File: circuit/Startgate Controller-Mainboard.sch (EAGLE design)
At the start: 22 parts, among them IC1 MAX3490ESA, IC2 L293D, U2 HEF4066BT, U3 HEF4066BT, U4 HEF4066BT, U5 HEF4066BT, X1 RJ45-8L21-B

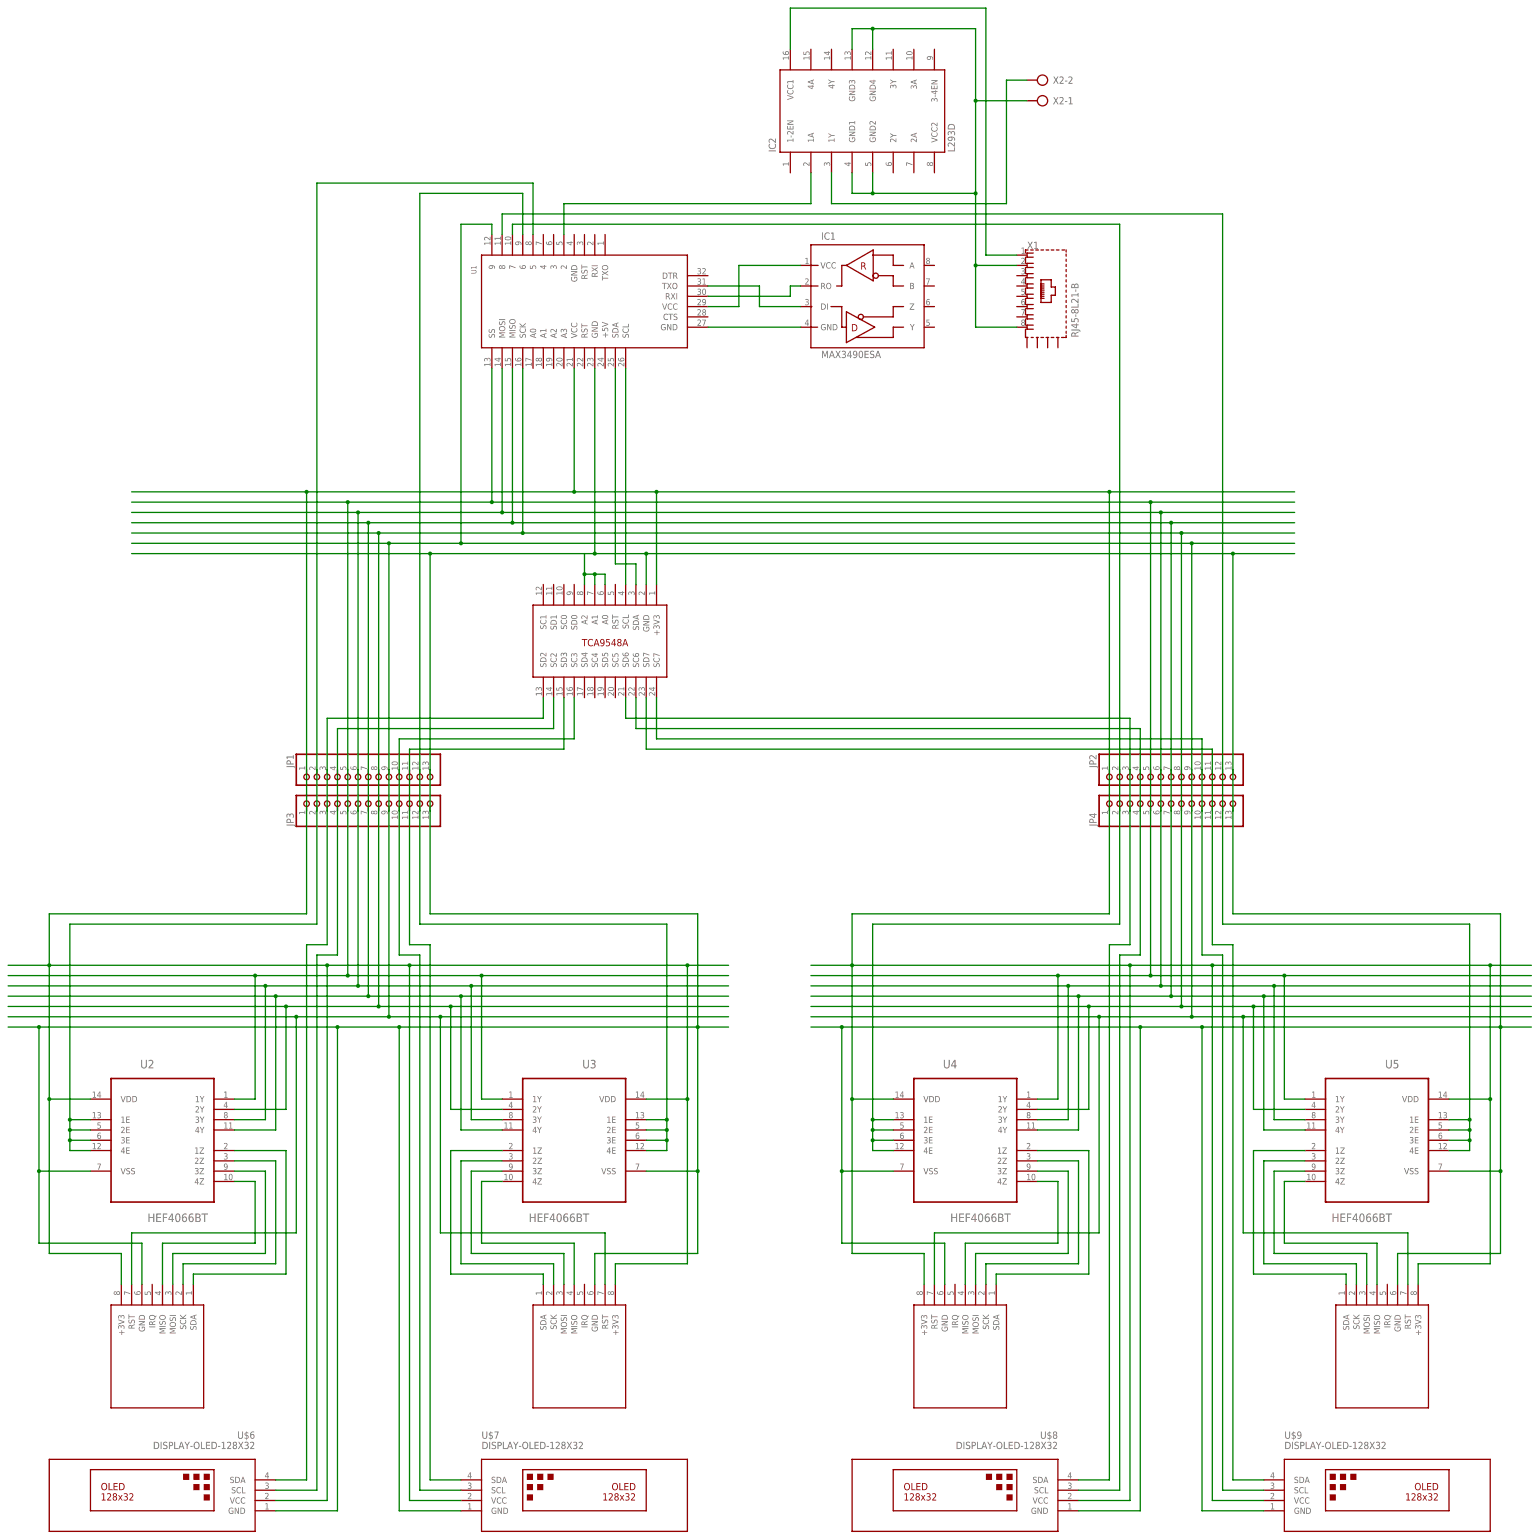
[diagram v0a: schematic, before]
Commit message: add the circuitry for the startgate main- and daughterboards
The main startgate controller has been split up into main board
and daughterboards, to make it easier to send them to the board house.
The two daughterboards should be identical, so the next iteration will
skip one.
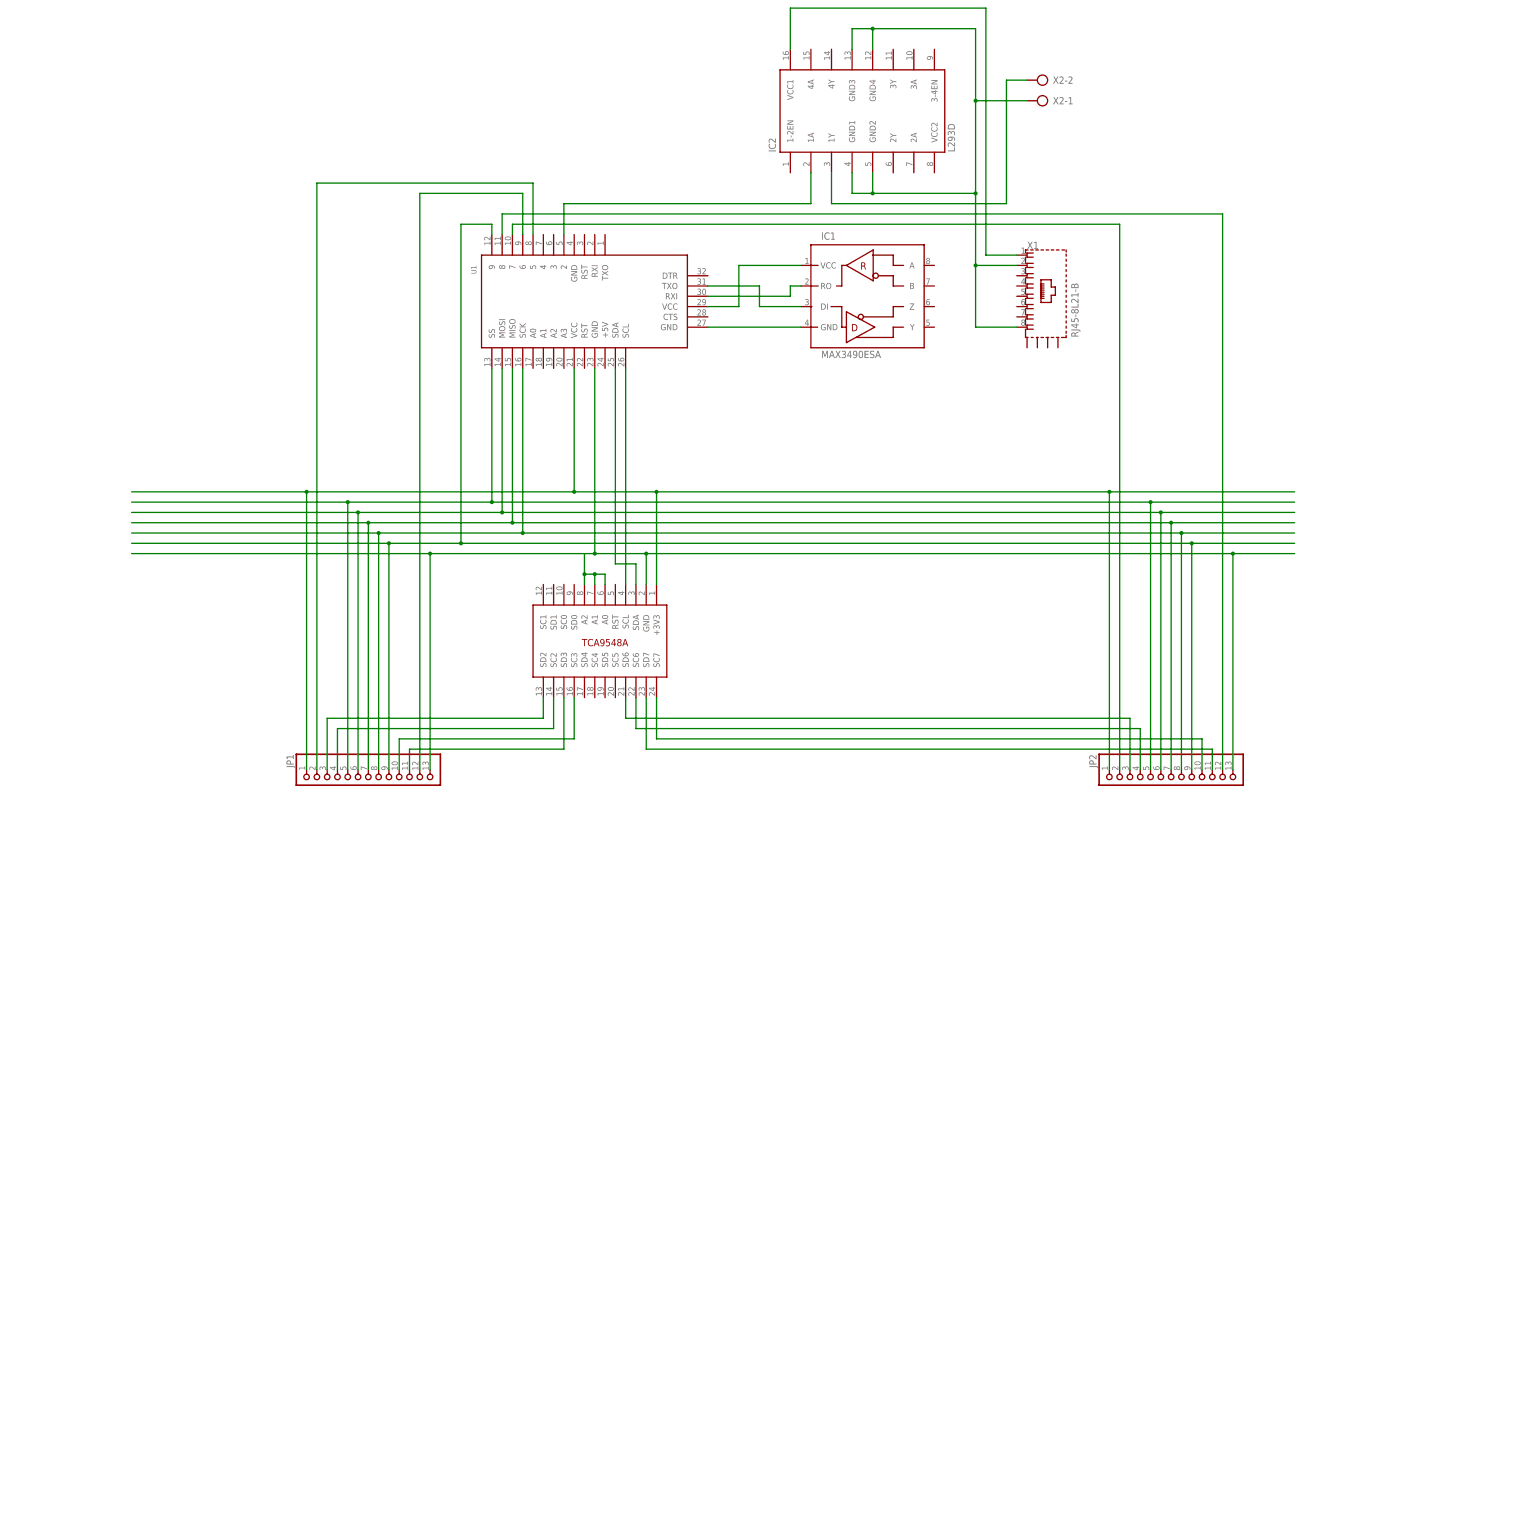
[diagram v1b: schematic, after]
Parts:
- removed JP3, JP4: (no value), pinhead:PINHD-1X13
- removed U$2, U$3, U$4, U$5: RFID-RC522, miro:RFID-RC522
- removed U$6, U$7, U$8, U$9: DISPLAY-OLED-128X32, diy-modules:DISPLAY-OLED-128X32
- removed U2, U3, U4, U5: HEF4066BT, NXP_By_element14_Batch_1:HEF4066BT
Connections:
- removed net MISO-OUT1: U$2.MISO, U2.4Z
- removed net MISO-OUT2: U$3.MISO, U3.4Z
- removed net MISO-OUT3: U$4.MISO, U4.4Z
- removed net MISO-OUT4: U$5.MISO, U5.4Z
- removed net MOSI-OUT1: U$2.MOSI, U2.3Z
- removed net MOSI-OUT2: U$3.MOSI, U3.3Z
- removed net MOSI-OUT3: U$4.MOSI, U4.3Z
- removed net MOSI-OUT4: U$5.MOSI, U5.3Z
- removed net SCK-OUT1: U$2.SCK, U2.2Z
- removed net SCK-OUT2: U$3.SCK, U3.2Z
- removed net SCK-OUT3: U$4.SCK, U4.2Z
- removed net SCK-OUT4: U$5.SCK, U5.2Z
- removed net SS-OUT1: U$2.SDA, U2.1Z
- removed net SS-OUT2: U$3.SDA, U3.1Z
- removed net SS-OUT3: U$4.SDA, U4.1Z
- removed net SS-OUT4: U$5.SDA, U5.1Z
- net +3V3: no longer JP3.1, JP4.1, U$2.+3V3, U$3.+3V3, U$4.+3V3, U$5.+3V3, U$6.VCC, U$7.VCC, U$8.VCC, U$9.VCC, U2.VDD, U3.VDD, U4.VDD, U5.VDD
- net ENA1: no longer JP3.2, U2.1E, U2.2E, U2.3E, U2.4E
- net ENA2: no longer JP3.12, U3.1E, U3.2E, U3.3E, U3.4E
- net ENA3: no longer JP4.2, U4.1E, U4.2E, U4.3E, U4.4E
- net ENA4: no longer JP4.12, U5.1E, U5.2E, U5.3E, U5.4E
- net GND: no longer JP3.13, JP4.13, U$2.GND, U$3.GND, U$4.GND, U$5.GND, U$6.GND, U$7.GND, U$8.GND, U$9.GND, U2.VSS, U3.VSS, U4.VSS, U5.VSS
- net MISO: no longer JP3.7, JP4.7, U2.4Y, U3.4Y, U4.4Y, U5.4Y
- net MOSI: no longer JP3.6, JP4.6, U2.3Y, U3.3Y, U4.3Y, U5.3Y
- net RST: no longer JP3.9, JP4.9, U$2.RST, U$3.RST, U$4.RST, U$5.RST
- net SCK: no longer JP3.8, JP4.8, U2.2Y, U3.2Y, U4.2Y, U5.2Y
- net SCL1: no longer JP3.4, U$6.SCL
- net SCL2: no longer JP3.10, U$7.SCL
- net SCL3: no longer JP4.4, U$8.SCL
- net SCL4: no longer JP4.10, U$9.SCL
- net SDA1: no longer JP3.3, U$6.SDA
- net SDA2: no longer JP3.11, U$7.SDA
- net SDA3: no longer JP4.3, U$8.SDA
- net SDA4: no longer JP4.11, U$9.SDA
- net SS: no longer JP3.5, JP4.5, U2.1Y, U3.1Y, U4.1Y, U5.1Y
